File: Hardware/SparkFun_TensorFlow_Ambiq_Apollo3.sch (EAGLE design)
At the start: 67 parts, among them J5 CORTEX_DEBUG, J7 CAMERA-HIMAX, U2 LIS2DH12, U3 1.8V, U5 ARTEMIS_MODULESMD, Y2 32.768kHz

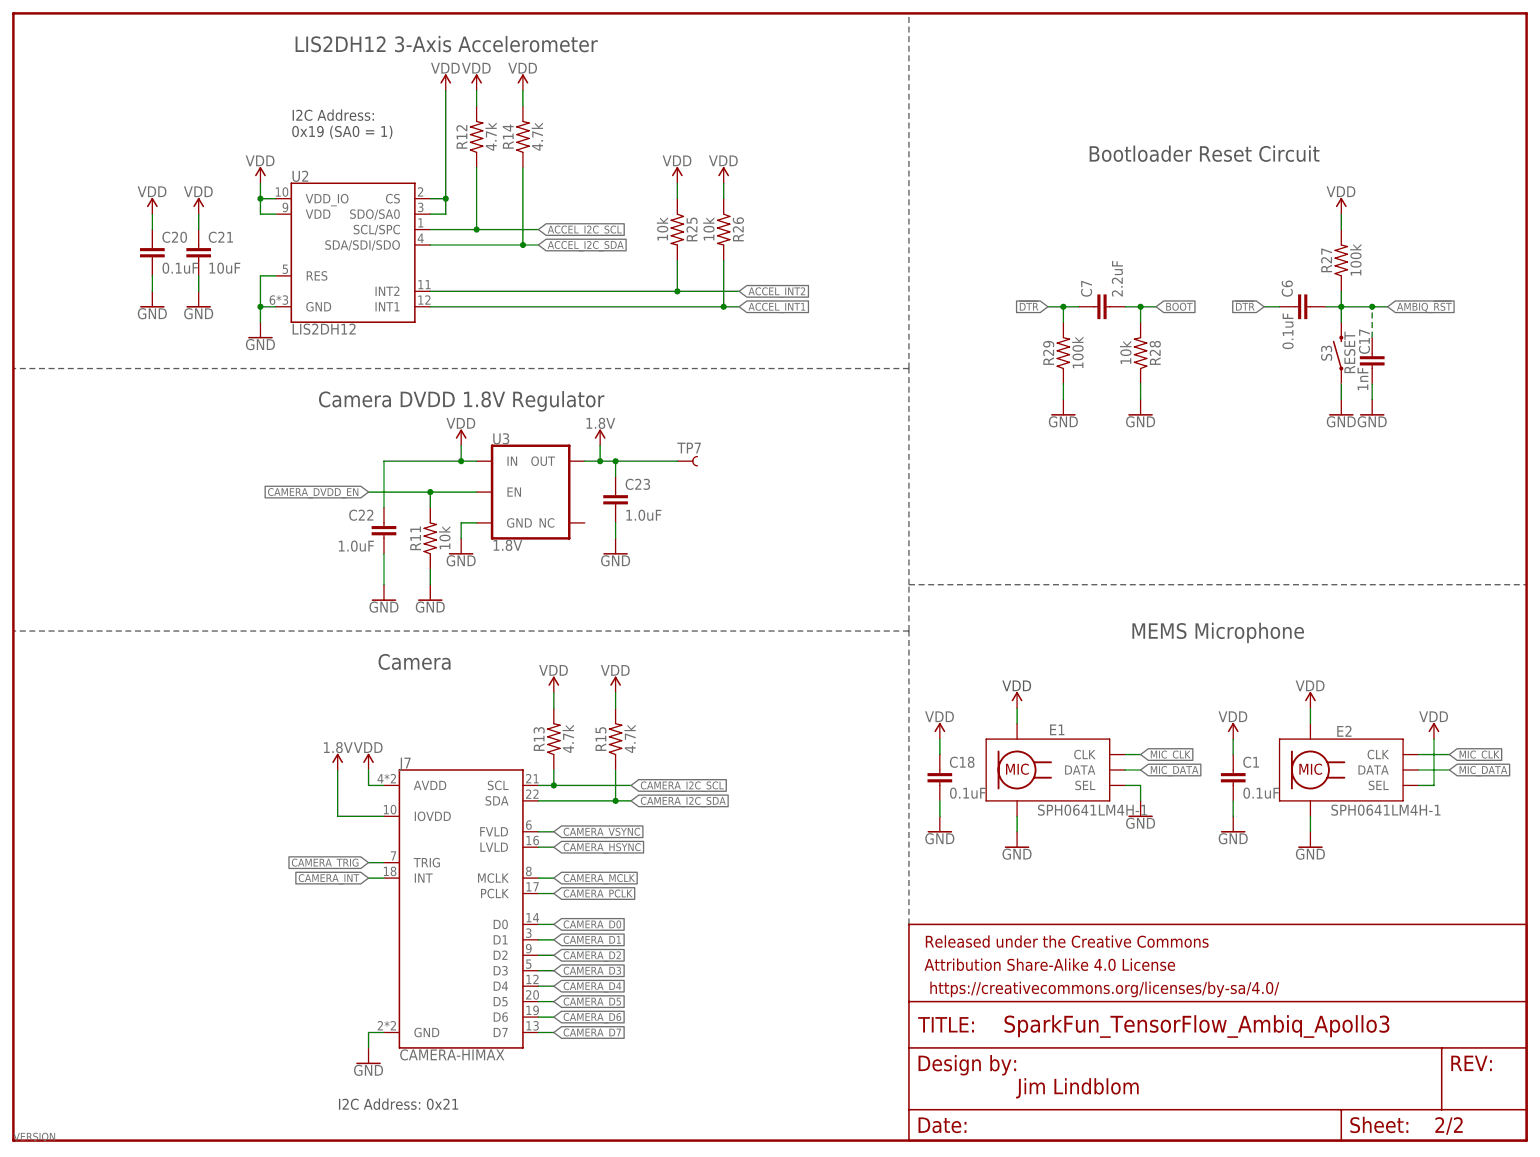
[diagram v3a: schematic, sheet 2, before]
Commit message: Change bootload circuit to use 0.1uF/220k standards.
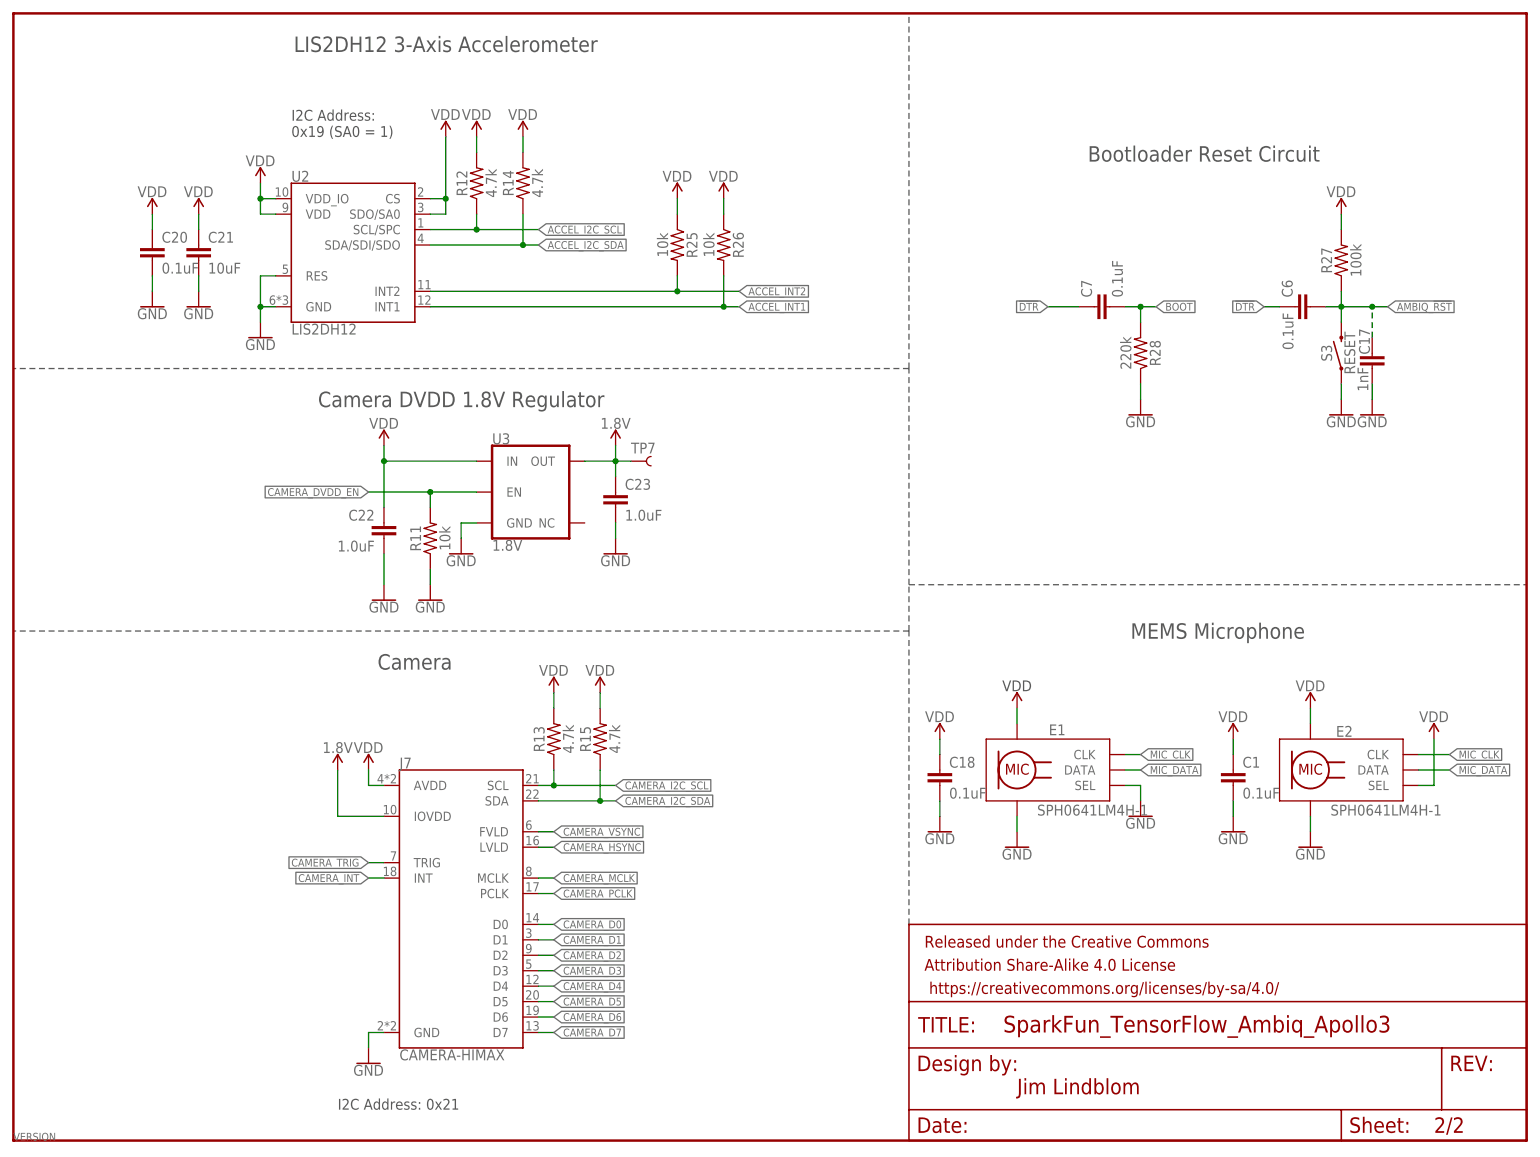
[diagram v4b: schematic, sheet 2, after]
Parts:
- removed R29: 100k, SparkFun-Resistors:100KOHM-0603-1/10W-1%
- C7: value 2.2uF -> 0.1uF; device SparkFun-Capacitors:2.2UF-0603-10V-20% -> SparkFun-Capacitors:0.1UF-0603-25V-(+80/-20%)
- R28: value 10k -> 220k; device SparkFun-Resistors:10KOHM-0603-1/10W-1% -> SparkFun-Resistors:220KOHM-0603-1/10W-1%
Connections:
- net !DTR: no longer R29.2
- net GND: no longer R29.1
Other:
- moved on the sheet: R12, R14, R15, R25, R26, TP3, TP4, TP7

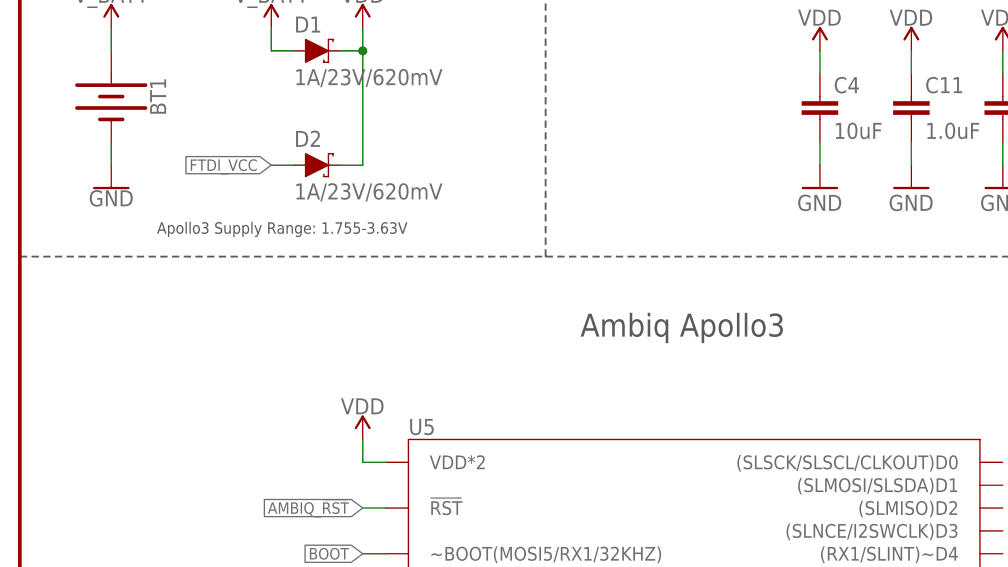
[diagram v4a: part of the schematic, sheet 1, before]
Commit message: Move parts to fill gap left by DNP resistor removal. Change text in sch from Apollo3 to Artemis.
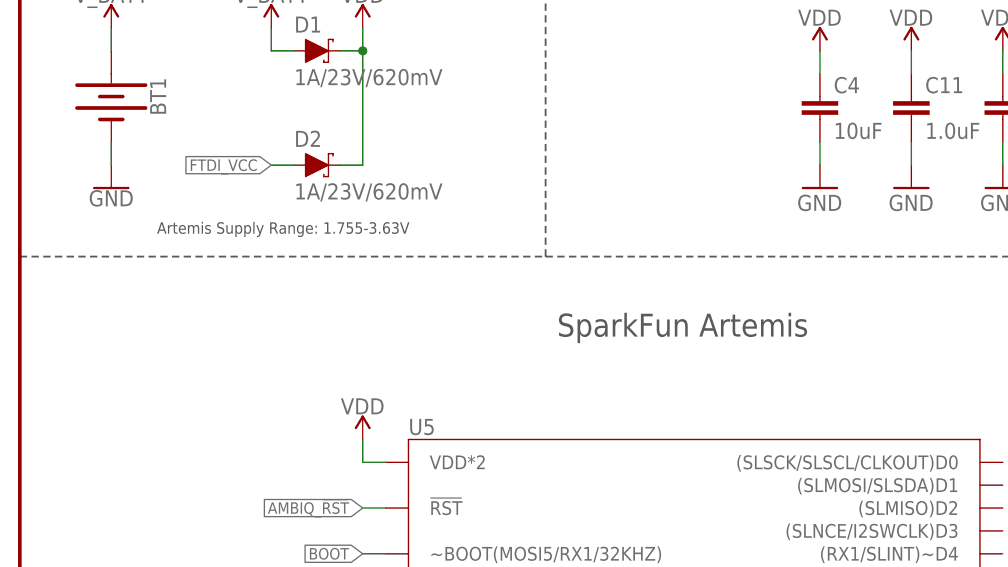
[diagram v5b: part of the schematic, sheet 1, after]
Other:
- note added: "Artemis Supply Range: 1.755-3.63V"
- note added: "SparkFun Artemis"
- note removed: "Ambiq Apollo3"
- note removed: "Apollo3 Supply Range: 1.755-3.63V"
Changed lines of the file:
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@@
 <text x="238.76" y="10.16" size="2.54" layer="94" align="top-left">v01</text>
 <text x="165.1" y="10.16" size="2.54" layer="94" align="top-left">Jim Lindblom</text>
-<text x="15.24" y="149.86" size="1.27" layer="97">Apollo3 Supply Range: 1.755-3.63V</text>
-<text x="73.66" y="139.7" size="2.54" layer="97" align="center">Ambiq Apollo3</text>
+<text x="15.24" y="149.86" size="1.27" layer="97">Artemis Supply Range: 1.755-3.63V</text>
+<text x="73.66" y="139.7" size="2.54" layer="97" align="center">SparkFun Artemis</text>
 <text x="30.48" y="180.34" size="2.54" layer="97" align="center">Coin Cell/Serial Power</text>
 <text x="99.06" y="180.34" size="2.54" layer="97" align="center">Artemis Decoupling</text>

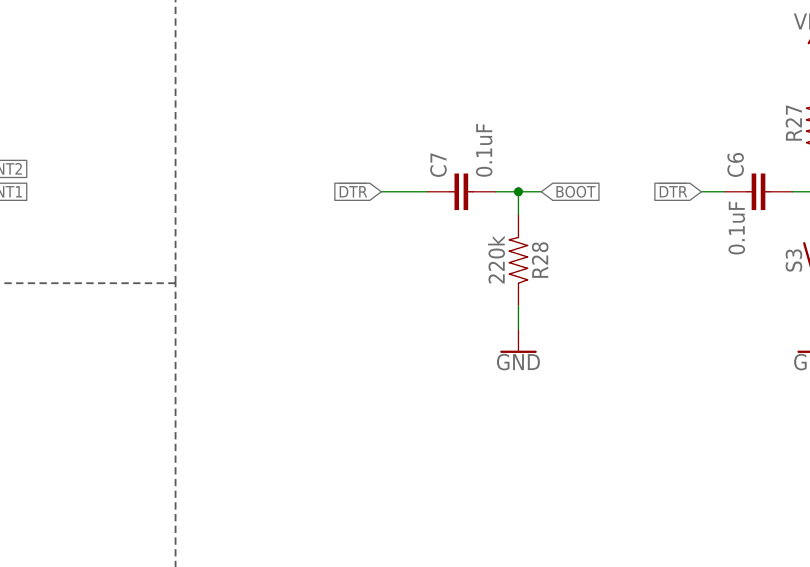
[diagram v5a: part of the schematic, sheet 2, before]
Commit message: Add DNP resistor back to design to match production boards.
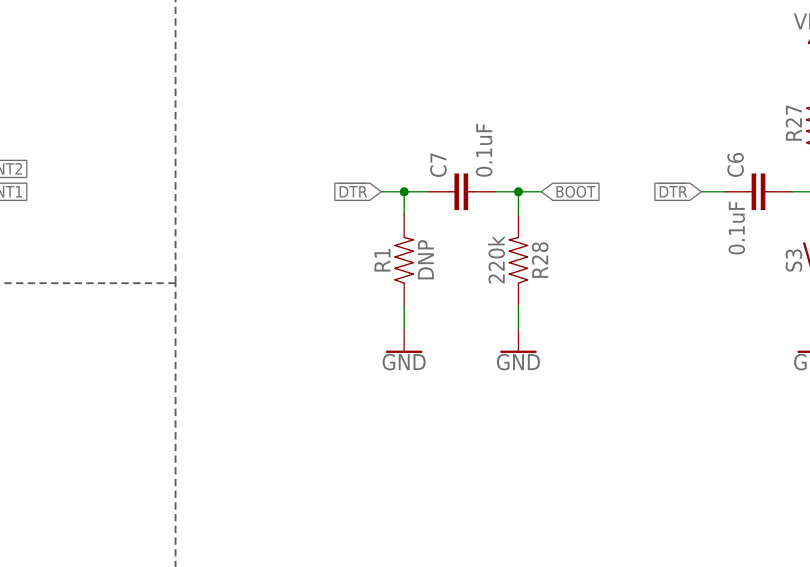
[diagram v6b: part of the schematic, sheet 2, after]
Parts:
- added R1: DNP, SparkFun-Resistors:100KOHM-0603-1/10W-1%
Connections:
- net !DTR: now also R1.2
- net GND: now also R1.1
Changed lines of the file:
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@@
 <?xml version="1.0" encoding="utf-8"?>
 <!DOCTYPE eagle SYSTEM "eagle.dtd">
-<eagle version="9.4.2">
+<eagle version="9.5.0">
 <drawing>
 <settings>
@@
 <part name="SUPPLY12" library="SparkFun-PowerSymbols" deviceset="VDD" device=""/>
 <part name="J7" library="SparkFun-Connectors" deviceset="CAMERA-HIMAX" device=""/>
+<part name="R1" library="SparkFun-Resistors" deviceset="100KOHM" device="-0603-1/10W-1%" value="DNP"/>
+<part name="GND9" library="SparkFun-PowerSymbols" deviceset="GND" device=""/>
 </parts>
 <sheets>
@@
 <attribute name="VALUE" x="63.5" y="14.986" size="1.778" layer="96" align="top-left"/>
 </instance>
+<instance part="R1" gate="G$1" x="172.72" y="129.54" smashed="yes" rot="R90">
+<attribute name="NAME" x="171.196" y="129.54" size="1.778" layer="95" font="vector" rot="R90" align="bottom-center"/>
+<attribute name="VALUE" x="174.244" y="129.54" size="1.778" layer="96" font="vector" rot="R90" align="top-center"/>
+</instance>
+<instance part="GND9" gate="1" x="172.72" y="119.38" smashed="yes" rot="MR0">
+<attribute name="VALUE" x="172.72" y="119.126" size="1.778" layer="96" rot="MR0" align="top-center"/>
+</instance>
 </instances>
 <busses>
@@
 <wire x1="213.36" y1="53.34" x2="213.36" y2="50.8" width="0.1524" layer="91"/>
 <pinref part="GND8" gate="1" pin="GND"/>
+</segment>
+<segment>
+<pinref part="R1" gate="G$1" pin="1"/>
+<pinref part="GND9" gate="1" pin="GND"/>
+<wire x1="172.72" y1="121.92" x2="172.72" y2="124.46" width="0.1524" layer="91"/>
 </segment>
 </net>
@@
 <label x="170.18" y="137.16" size="1.27" layer="95" rot="MR0" xref="yes"/>
 <pinref part="C7" gate="G$1" pin="1"/>
-<wire x1="175.26" y1="137.16" x2="170.18" y2="137.16" width="0.1524" layer="91"/>
-</segment>
-<segment>
+<wire x1="175.26" y1="137.16" x2="172.72" y2="137.16" width="0.1524" layer="91"/>
+<pinref part="R1" gate="G$1" pin="2"/>
+<wire x1="172.72" y1="137.16" x2="170.18" y2="137.16" width="0.1524" layer="91"/>
+<wire x1="172.72" y1="134.62" x2="172.72" y2="137.16" width="0.1524" layer="91"/>
+<junction x="172.72" y="137.16"/>
+</segment>
+<segment>
